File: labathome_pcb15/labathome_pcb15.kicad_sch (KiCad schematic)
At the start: 41 parts, among them J11 USB_ESP32, J15 CAN RS 485, J17 Micro_SD_Card_Det1, J21 GPIO, J22 Volts, J6 I2C, J7 PROG ESP, SW2 YELLOW, SW3 GREEN, SW3 Reset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

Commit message: bsec
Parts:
- added X2: Display_1.3inch, liebler_OPTO:IPS_130, symbol liebler_OPTO:Display_LH154K-PG04
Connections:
- net +3V3: now also X2.2 (LEDK), X2.4 (VDD)
- net GND: now also X2.1 (GND), X2.12 (GND), X2.5 (GND), X2.6 (GND), X2.8 (CS)
- net LCD_BACKLIGHT: now also X2.3 (LEDA)
- net LCD_CLK: now also X2.9 (SCL)
- net LCD_DAT: now also X2.10 (SDA)
- net LCD_DC: now also X2.7 (DC)
- net LCD_RES: now also X2.11 (RESET)

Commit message: TPS2116
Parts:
- removed U21: IPS_240_240, liebler_OPTO:IPS_240_240_1.3, symbol liebler_OPTO:IPS_240_240
- added Q6: IRLML6344, Package_TO_SOT_SMD:SOT-23, symbol Transistor_FET:IRLML0030
- added R74: 1k, Resistor_SMD:R_0402_1005Metric, symbol Device:R
- added R75: 10k, Resistor_SMD:R_0201_0603Metric, symbol Device:R
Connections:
- net GND: now also Q6.2 (S), R75.2
- net LCD_BACKLIGHT: now also U2.12 (GPIO8/TOUCH8/ADC1_CH7/SUBSPICS1), R74.2; no longer U2.31 (GPIO38/FSPIWP/SUBSPIWP), X2.3 (LEDA)
- net LCD_DAT: now also U2.31 (GPIO38/FSPIWP/SUBSPIWP); no longer U2.11 (GPIO18/U1RXD/ADC2_CH7/CLK_OUT3)
- net LCD_DC: now also U2.11 (GPIO18/U1RXD/ADC2_CH7/CLK_OUT3); no longer U2.12 (GPIO8/TOUCH8/ADC1_CH7/SUBSPICS1)
- net USB+ renamed USBP
- net USB- renamed USBM
- new net: Q6.1 (G), R74.1, R75.1
- new net: Q6.3 (D), X2.3 (LEDA)

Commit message: Labathome 15.2 as ordered at JLCPCB
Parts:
- added R78: 10R, Resistor_SMD:R_1206_3216Metric, symbol Device:R
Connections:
- net LCD_BACKLIGHT: now also U2.10 (GPIO17/U1TXD/ADC2_CH6); no longer U2.12 (GPIO8/TOUCH8/ADC1_CH7/SUBSPICS1)
- net LCD_CLK: now also U2.12 (GPIO8/TOUCH8/ADC1_CH7/SUBSPICS1); no longer U2.10 (GPIO17/U1TXD/ADC2_CH6)
- net at Q6.3 (D): now also R78.2; no longer X2.3 (LEDA)
- new net: R78.1, X2.3 (LEDA)
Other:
- moved on the sheet: Q6, R74, R75
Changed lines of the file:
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@@
 	)
 	(junction
-		(at 129.54 185.42)
+		(at 129.54 191.77)
 		(diameter 0)
 		(color 0 0 0 0)
@@
 	)
 	(junction
-		(at 121.92 177.8)
+		(at 121.92 184.15)
 		(diameter 0)
 		(color 0 0 0 0)
@@
 	(wire
 		(pts
+			(xy 134.62 171.45) (xy 129.54 171.45)
+		)
+		(stroke
+			(width 0)
+			(type default)
+		)
+	)
+	(wire
+		(pts
+			(xy 148.59 152.4) (xy 134.62 152.4)
+		)
+		(stroke
+			(width 0)
+			(type default)
+		)
+	)
+	(wire
+		(pts
 			(xy 234.95 41.91) (xy 233.68 41.91)
 		)
@@
 	(wire
 		(pts
+			(xy 134.62 152.4) (xy 134.62 171.45)
+		)
+		(stroke
+			(width 0)
+			(type default)
+		)
+	)
+	(wire
+		(pts
 			(xy 180.34 60.96) (xy 187.96 60.96)
 		)
@@
 	(wire
 		(pts
+			(xy 19.05 118.11) (xy 20.32 118.11)
+		)
+		(stroke
+			(width 0)
+			(type default)
+		)
+	)
+	(wire
+		(pts
 			(xy 85.09 113.03) (xy 83.82 113.03)
 		)
@@
 	(wire
 		(pts
-			(xy 121.92 185.42) (xy 129.54 185.42)
-		)
-		(stroke
-			(width 0)
-			(type default)
-		)
-	)
-	(wire
-		(pts
-			(xy 19.05 118.11) (xy 31.75 118.11)
+			(xy 121.92 191.77) (xy 129.54 191.77)
 		)
 		(stroke
@@
 	(wire
 		(pts
-			(xy 129.54 182.88) (xy 129.54 185.42)
+			(xy 129.54 189.23) (xy 129.54 191.77)
 		)
 		(stroke
@@
 	(wire
 		(pts
-			(xy 129.54 152.4) (xy 148.59 152.4)
-		)
-		(stroke
-			(width 0)
-			(type default)
-		)
-	)
-	(wire
-		(pts
 			(xy 111.76 148.59) (xy 115.57 148.59)
 		)
@@
 	(wire
 		(pts
-			(xy 129.54 172.72) (xy 129.54 152.4)
-		)
-		(stroke
-			(width 0)
-			(type default)
-		)
-	)
-	(wire
-		(pts
 			(xy 100.33 115.57) (xy 100.33 113.03)
 		)
@@
 	(global_label "LCD_BACKLIGHT"
 		(shape output)
-		(at 38.1 53.34 180)
+		(at 38.1 76.2 180)
 		(fields_autoplaced yes)
 		(effects
@@
 		)
 		(property "Intersheetrefs" "${INTERSHEET_REFS}"
-			(at 20.4795 53.34 0)
+			(at 20.4795 76.2 0)
 			(effects
 				(font
@@
 	(global_label "LCD_CLK"
 		(shape output)
-		(at 38.1 76.2 180)
+		(at 38.1 53.34 180)
 		(fields_autoplaced yes)
 		(effects
@@
 		)
 		(property "Intersheetrefs" "${INTERSHEET_REFS}"
-			(at 27.011 76.2 0)
+			(at 27.011 53.34 0)
 			(effects
 				(font
@@
 	(global_label "LCD_BACKLIGHT"
 		(shape input)
-		(at 121.92 170.18 180)
+		(at 121.92 176.53 180)
 		(fields_autoplaced yes)
 		(effects
@@
 		)
 		(property "Intersheetrefs" "${INTERSHEET_REFS}"
-			(at 104.2995 170.18 0)
+			(at 104.2995 176.53 0)
 			(effects
 				(font
@@
 	(global_label "LCD_RES"
 		(shape input)
-		(at 19.05 118.11 180)
+		(at 20.32 118.11 0)
 		(fields_autoplaced yes)
 		(effects
@@
 				(size 1.27 1.27)
 			)
-			(justify right)
+			(justify left)
 		)
 		(property "Intersheetrefs" "${INTERSHEET_REFS}"
-			(at 7.9006 118.11 0)
+			(at 31.4694 118.11 0)
 			(effects
 				(font
 					(size 1.27 1.27)
 				)
-				(justify right)
+				(justify left)
 				(hide yes)
 			)
@@
 	(symbol
 		(lib_id "Transistor_FET:IRLML0030")
-		(at 127 177.8 0)
+		(at 127 184.15 0)
 		(unit 1)
 		(exclude_from_sim no)
@@
 		(dnp no)
 		(property "Reference" "Q6"
-			(at 125.73 172.72 0)
+			(at 125.73 179.07 0)
 			(effects
 				(font
@@
 		)
 		(property "Value" "IRLML6344"
-			(at 133.35 184.15 90)
+			(at 133.35 190.5 90)
 			(effects
 				(font
@@
 		)
 		(property "Footprint" "Package_TO_SOT_SMD:SOT-23"
-			(at 132.08 179.705 0)
+			(at 132.08 186.055 0)
 			(effects
 				(font
@@
 		)
 		(property "Datasheet" "https://www.infineon.com/dgdl/irlml0030pbf.pdf?fileId=5546d462533600a401535664773825df"
-			(at 127 177.8 0)
+			(at 127 184.15 0)
 			(effects
 				(font
@@
 		)
 		(property "Description" "5.3A Id, 30V Vds, 27mOhm Rds, N-Channel HEXFET Power MOSFET, SOT-23"
-			(at 127 177.8 0)
+			(at 127 184.15 0)
 			(effects
 				(font
@@
 	(symbol
 		(lib_id "Device:R")
-		(at 121.92 181.61 0)
+		(at 121.92 187.96 0)
 		(unit 1)
 		(exclude_from_sim no)
@@
 		(dnp no)
 		(property "Reference" "R75"
-			(at 116.84 181.61 0)
+			(at 116.84 187.96 0)
 			(effects
 				(font
@@
 		)
 		(property "Value" "10k"
-			(at 121.92 181.61 90)
+			(at 121.92 187.96 90)
 			(effects
 				(font
@@
 		)
 		(property "Footprint" "Resistor_SMD:R_0201_0603Metric"
-			(at 120.142 181.61 90)
+			(at 120.142 187.96 90)
 			(effects
 				(font
@@
 		)
 		(property "Datasheet" "~"
-			(at 121.92 181.61 0)
+			(at 121.92 187.96 0)
 			(effects
 				(font
@@
 		)
 		(property "Description" ""
-			(at 121.92 181.61 0)
+			(at 121.92 187.96 0)
 			(effects
 				(font
@@
 	)
 	(symbol
+		(lib_id "Device:R")
+		(at 129.54 175.26 0)
+		(unit 1)
+		(exclude_from_sim no)
+		(in_bom yes)
+		(on_board yes)
+		(dnp no)
+		(property "Reference" "R78"
+			(at 125.73 175.26 0)
+			(effects
+				(font
+					(size 1.27 1.27)
+				)
+			)
+		)
+		(property "Value" "10R"
+			(at 129.54 175.26 90)
+			(effects
+				(font
+					(size 1.27 1.27)
+				)
+			)
+		)
+		(property "Footprint" "Resistor_SMD:R_1206_3216Metric"
+			(at 127.762 175.26 90)
+			(effects
+				(font
+					(size 1.27 1.27)
+				)
+				(hide yes)
+			)
+		)
+		(property "Datasheet" "~"
+			(at 129.54 175.26 0)
+			(effects
+				(font
+					(size 1.27 1.27)
+				)
+				(hide yes)
+			)
+		)
+		(property "Description" ""
+			(at 129.54 175.26 0)
+			(effects
+				(font
+					(size 1.27 1.27)
+				)
+				(hide yes)
+			)
+		)
+		(pin "1"
+		)
+		(pin "2"
+		)
+		(instances
+			(project "labathome_pcb15"
+				(path "/e4d6926a-1a8b-424d-97c4-66b6ad87e4ac"
+					(reference "R78")
+					(unit 1)
+				)
+			)
+		)
+	)
+	(symbol
 		(lib_id "power:GND")
 		(at 201.93 133.35 0)
@@
 	(symbol
 		(lib_id "power:GND")
-		(at 129.54 185.42 90)
+		(at 129.54 191.77 90)
 		(unit 1)
 		(exclude_from_sim no)
@@
 		(dnp no)
 		(property "Reference" "#PWR0138"
-			(at 135.89 185.42 0)
+			(at 135.89 191.77 0)
 			(effects
 				(font
@@
 		)
 		(property "Value" "GND"
-			(at 134.366 185.42 90)
+			(at 134.366 191.77 90)
 			(effects
 				(font
@@
 		)
 		(property "Footprint" ""
-			(at 129.54 185.42 0)
+			(at 129.54 191.77 0)
 			(effects
 				(font
@@
 		)
 		(property "Datasheet" ""
-			(at 129.54 185.42 0)
+			(at 129.54 191.77 0)
 			(effects
 				(font
@@
 		)
 		(property "Description" "Power symbol creates a global label with name \"GND\" , ground"
-			(at 129.54 185.42 0)
+			(at 129.54 191.77 0)
 			(effects
 				(font
@@
 	(symbol
 		(lib_id "Device:R")
-		(at 121.92 173.99 180)
+		(at 121.92 180.34 180)
 		(unit 1)
 		(exclude_from_sim no)
@@
 		(dnp no)
 		(property "Reference" "R74"
-			(at 124.46 173.99 90)
+			(at 124.46 180.34 90)
 			(effects
 				(font
@@
 		)
 		(property "Value" "1k"
-			(at 121.92 173.99 90)
+			(at 121.92 180.34 90)
 			(effects
 				(font
@@
 		)
 		(property "Footprint" "Resistor_SMD:R_0402_1005Metric"
-			(at 123.698 173.99 90)
+			(at 123.698 180.34 90)
 			(effects
 				(font
@@
 		)
 		(property "Datasheet" "~"
-			(at 121.92 173.99 0)
+			(at 121.92 180.34 0)
 			(effects
 				(font
@@
 		)
 		(property "Description" ""
-			(at 121.92 173.99 0)
+			(at 121.92 180.34 0)
 			(effects
 				(font

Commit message: Fixes for 15.2 and 15.ß
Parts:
- added C67: 1u, Capacitor_SMD:C_0402_1005Metric, symbol Device:C
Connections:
- net +3V3: now also X2.3 (LEDA), C67.2; no longer X2.2 (LEDK)
- net GND: now also C67.1
- net at R78.1: now also X2.2 (LEDK); no longer X2.3 (LEDA)
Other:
- moved on the sheet: C27

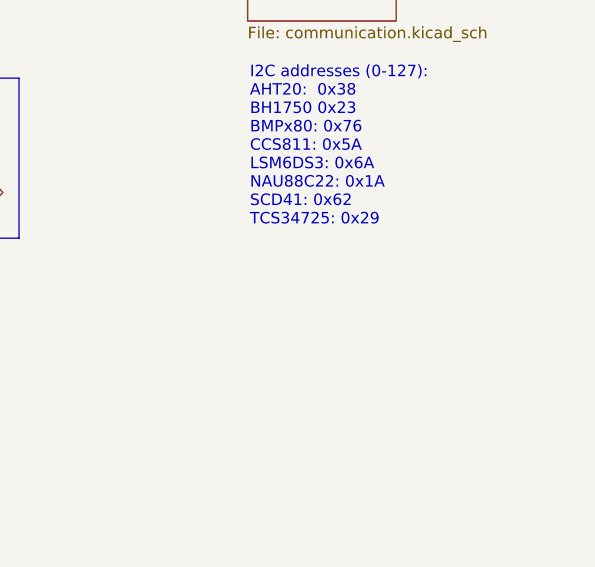
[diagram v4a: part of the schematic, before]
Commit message: Added Stepper Motors (initial)
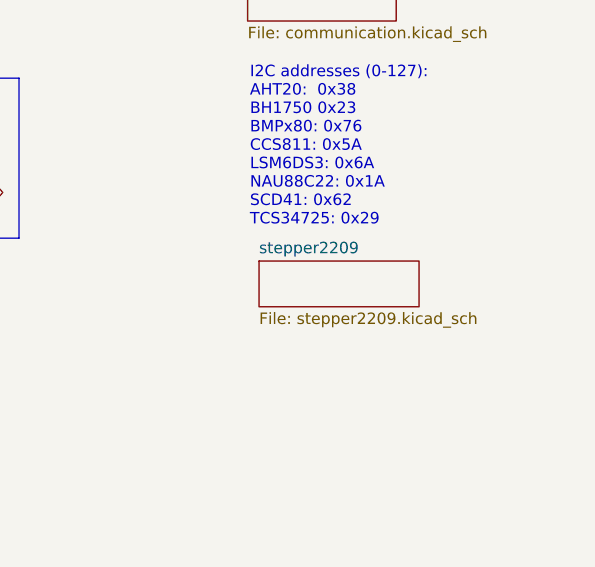
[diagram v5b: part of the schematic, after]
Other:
- added sheet stepper2209 (stepper2209.kicad_sch)
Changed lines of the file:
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@@
+	)
+	(sheet
+		(at 242.57 97.79)
+		(size 17.78 5.08)
+		(fields_autoplaced yes)
+		(stroke
+			(width 0.1524)
+			(type solid)
+		)
+		(fill
+			(color 0 0 0 0.0000)
+		)
+		(property "Sheetname" "stepper2209"
+			(at 242.57 97.0784 0)
+			(effects
+				(font
+					(size 1.27 1.27)
+				)
+				(justify left bottom)
+			)
+		)
+		(property "Sheetfile" "stepper2209.kicad_sch"
+			(at 242.57 103.4546 0)
+			(effects
+				(font
+					(size 1.27 1.27)
+				)
+				(justify left top)
+			)
+		)
+		(instances
+			(project "labathome_pcb15"
+				(path "/e4d6926a-1a8b-424d-97c4-66b6ad87e4ac"
+					(page "8")
+				)
+			)
+		)
 	)
 	(sheet

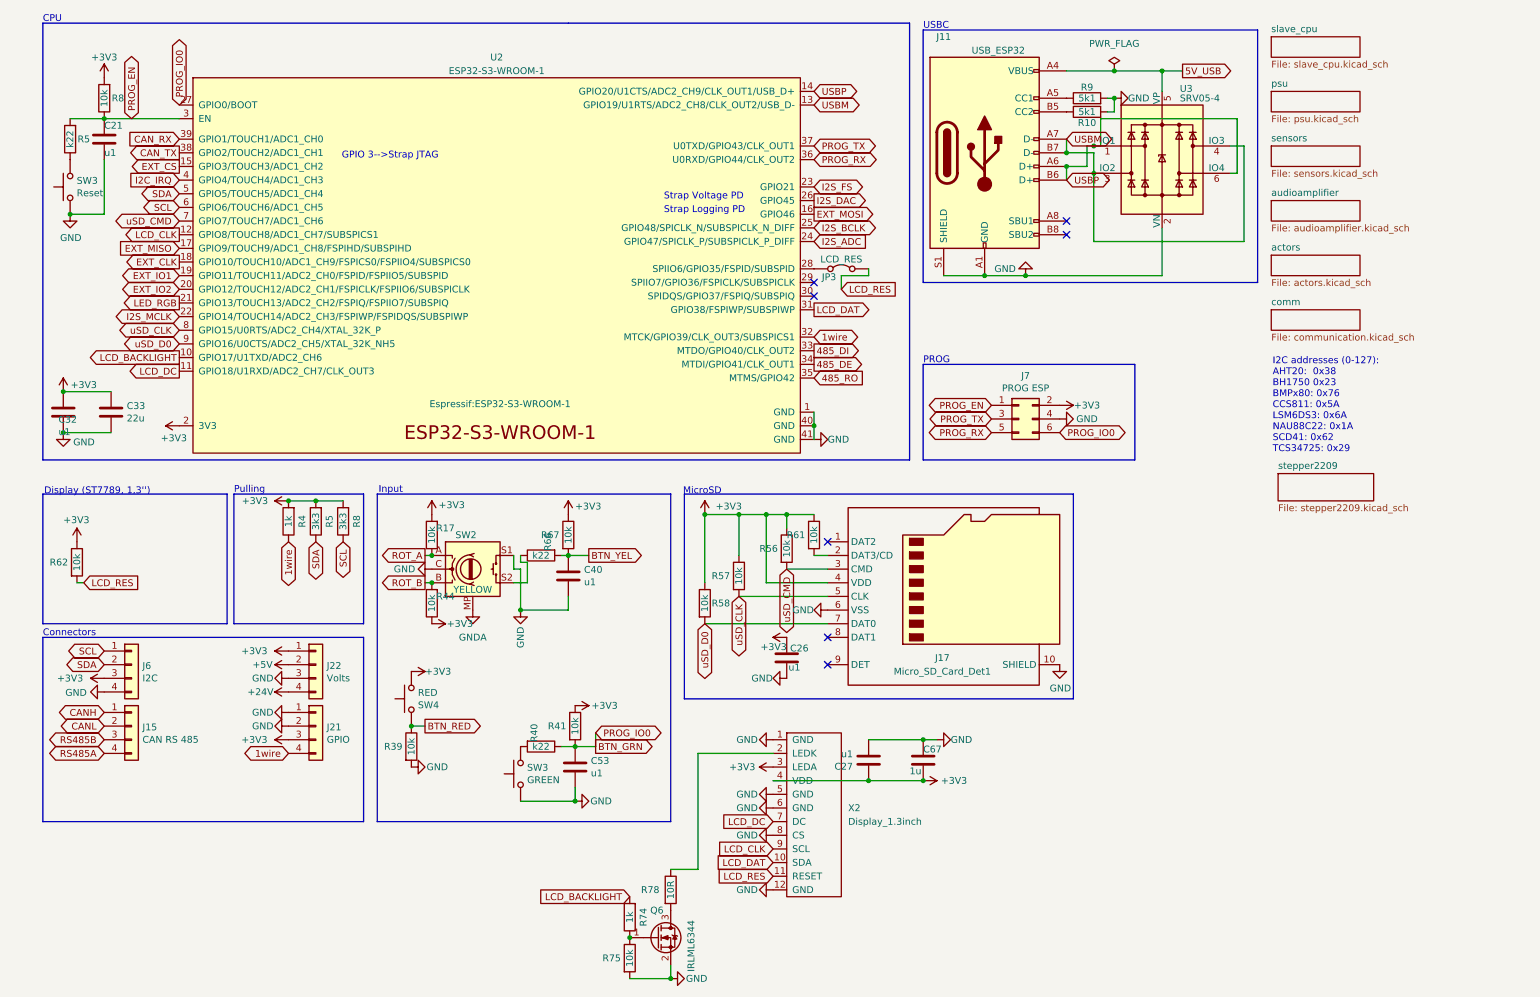
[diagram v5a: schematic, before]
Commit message: PCB update; DRC check passed; optimized routing
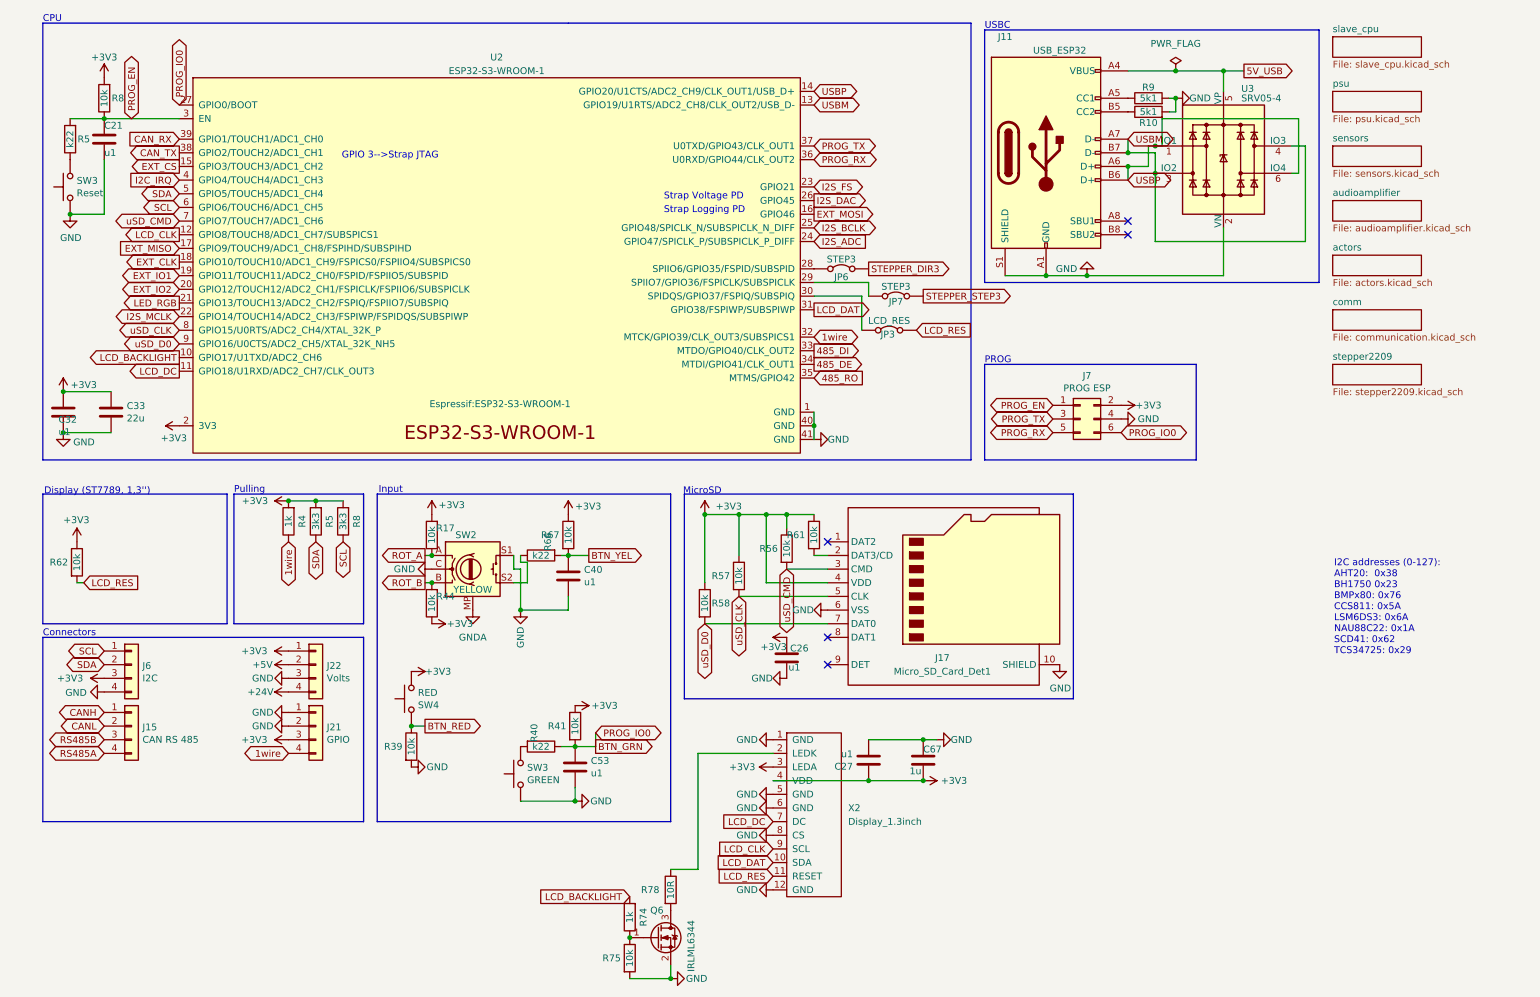
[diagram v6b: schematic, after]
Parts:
- added JP6, JP7: STEP3, Jumper:SolderJumper-2_P1.3mm_Bridged2Bar_RoundedPad1.0x1.5mm, symbol Jumper:Jumper_2_Bridged
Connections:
- net at U2.28 (SPIIO6/GPIO35/FSPID/SUBSPID): now also JP6.1 (A); no longer JP3.1 (A)
- net at U2.29 (SPIIO7/GPIO36/FSPICLK/SUBSPICLK): now also JP7.1 (A)
- net at U2.30 (SPIDQS/GPIO37/FSPIQ/SUBSPIQ): now also JP3.1 (A)
- new net STEPPER_DIR3: JP6.2 (B)
- new net STEPPER_STEP3: JP7.2 (B)
- no-connect marks 7 -> 5
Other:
- moved on the sheet: J11, J7, JP3, R10, R9, U3

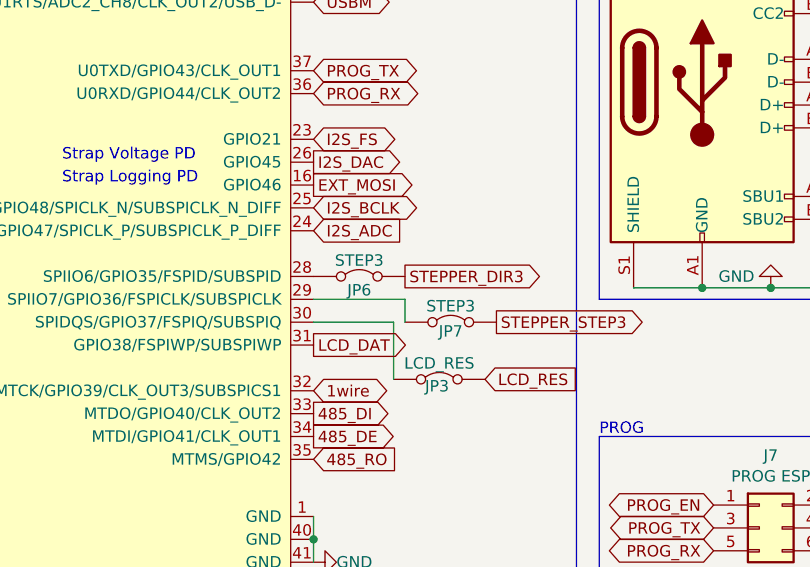
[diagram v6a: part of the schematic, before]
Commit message: Layout improvement; use common enable signal for steppers
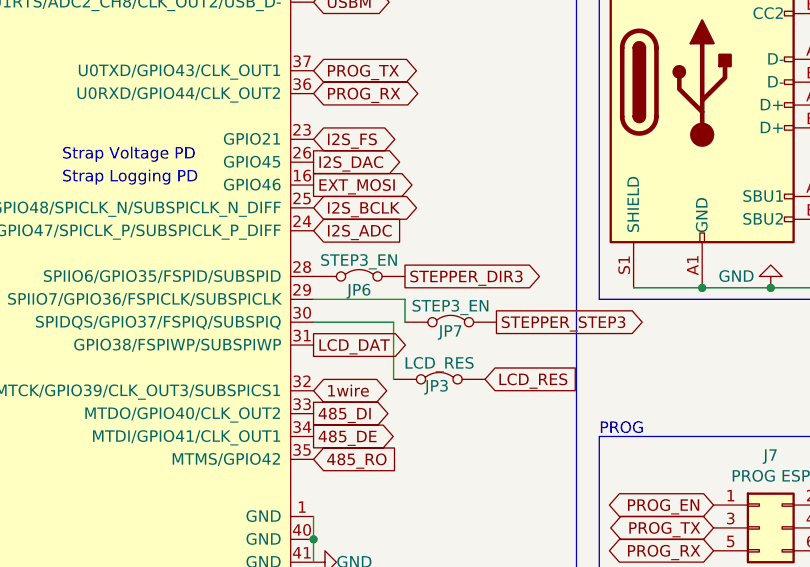
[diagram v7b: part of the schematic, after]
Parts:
- JP6, JP7: value STEP3 -> STEP3_EN
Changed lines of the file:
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@@
 			)
 		)
-		(property "Value" "STEP3"
+		(property "Value" "STEP3_EN"
 			(at 161.29 57.912 0)
 			(effects
@@
 			)
 		)
-		(property "Value" "STEP3"
+		(property "Value" "STEP3_EN"
 			(at 171.45 62.992 0)
 			(effects
